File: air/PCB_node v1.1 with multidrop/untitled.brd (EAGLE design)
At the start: 150 x 100 mm, 113 parts, among them J1 10118193-0001LF, J2 10118193-0001LF, K1 351, K2 351, K3 SRD-05VDC-SL-C, K4 351, Q1 MMBT3904, Q10 S9013, Q2 MMBT3904, Q3 12MHz, Q4 S9013, Q5 S9013, Q6 S9013, Q7 12MHz, Q8 MMBT3904, Q9 MMBT3904, U1 CH340G, U10 ADS1115IDGSR, U11 PC817X2NIP0F, U2 ESP32-WROOM-32D, U3 AMS1117, U4 PC817X2NIP0F, U5 PC817X2NIP0F, U6 PC817X2NIP0F, U7 CH340G, U8 AMS1117, U9 ESP32-WROOM-32D, X1 MSTBA2, X2 MSTBA2, X3 MSTBA4, X4 MSTBA3, X5 MSTBA2, X6 MSTBA4, X7 C-GRID-02-70543, X8 MSTBA2

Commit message: menambah GPS chip
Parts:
- added C22: 27nH, rcl:C0805K
- added C23: 10nF, rcl:C0805K
- added D16: SML-LXT0805IW-TR, SML-LXT0805IW-TR:LEDC2012X120N
- added J3: U.FL-R-SMT(01), U.FL-R-SMT_01_:HRS_U.FL-R-SMT(01)
- added Q11: PDTC114EU,115, PDTC114EU_115:SOT65P210X110-3N
- added R32: 10, rcl:M0805
- added R33: 1k, rcl:M0805
- added U12: NEO-M8N-0, NEO-M8N-0:XCVR_NEO-M8N-0
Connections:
- new net N$36: C22.1, C23.1, R32.2
- new net N$37: R32.1, U12.9
- new net N$38: D16.C, Q11.3
- new net N$39: D16.A, R33.1
- new net RF_IN: C22.2, J3.3, U12.11
- new net TIMEPULSE: Q11.1, U12.3
- new net VDD_USB: U12.7
- new net V_BCKP: U12.22
- net GND: now also C23.2, J3.1, J3.2, Q11.2, U12.10, U12.12, U12.13, U12.24
- net RX_GPS: now also U12.21
- net TX_GPS: now also U12.20
- net VCC1: now also R33.2, U12.23
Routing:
- net VCC1: track 168.0 -> 321.5 mm, vias 5 -> 8
- net GND: track 987.7 -> 1077.9 mm, vias 14 -> 17
- net RF_IN: track 0.00 -> 50.8 mm, vias 0 -> 2
- net TX_GPS: track 241.9 -> 271.1 mm, vias 0 -> 1
- net N$37: track 0.00 -> 24.6 mm, vias 0 -> 2
- net TIMEPULSE: track 0.00 -> 23.8 mm
- net RX_GPS: track 246.0 -> 263.4 mm, vias 0 -> 1
- net N$36: track 0.00 -> 14.1 mm, vias 0 -> 2
- net A0: track 92.9 -> 101.9 mm
- net CYBLE2: track 157.7 -> 166.1 mm
- net CYBLE1: track 161.2 -> 169.2 mm
- net CYBLE3: track 120.6 -> 128.5 mm
- net CYBLE5: track 146.1 -> 153.1 mm
- net SCL1: track 286.6 -> 281.6 mm
- net N$38: track 0.00 -> 3.83 mm
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
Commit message: fix PCB
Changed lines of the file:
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@@
 <wire x1="108.07954375" y1="30.049675" x2="105.128484375" y2="30.049675" width="0.2032" layer="1"/>
 <wire x1="105.128484375" y1="30.049675" x2="104.565653125" y2="30.61250625" width="0.2032" layer="1"/>
-<wire x1="104.565653125" y1="30.61250625" x2="104.565653125" y2="33.55030625" width="0.2032" layer="1"/>
-<wire x1="103.640440625" y1="34.47551875" x2="102.309053125" y2="34.47551875" width="0.2032" layer="1"/>
-<wire x1="104.565653125" y1="33.55030625" x2="103.640440625" y2="34.47551875" width="0.2032" layer="1"/>
+<wire x1="104.565653125" y1="30.61250625" x2="104.565653125" y2="33.85510625" width="0.2032" layer="1"/>
+<wire x1="103.945240625" y1="34.47551875" x2="102.309053125" y2="34.47551875" width="0.2032" layer="1"/>
+<wire x1="104.565653125" y1="33.85510625" x2="103.945240625" y2="34.47551875" width="0.2032" layer="1"/>
 <wire x1="120.04408125" y1="34.495728125" x2="115.568690625" y2="34.495728125" width="0.2032" layer="1"/>
 <wire x1="115.568690625" y1="34.495728125" x2="113.475909375" y2="36.588509375" width="0.2032" layer="1"/>
 <wire x1="113.475909375" y1="36.588509375" x2="108.2684125" y2="36.588509375" width="0.2032" layer="1"/>
-<wire x1="106.155421875" y1="34.47551875" x2="103.640440625" y2="34.47551875" width="0.2032" layer="1"/>
+<wire x1="106.155421875" y1="34.47551875" x2="103.945240625" y2="34.47551875" width="0.2032" layer="1"/>
 <wire x1="108.2684125" y1="36.588509375" x2="106.155421875" y2="34.47551875" width="0.2032" layer="1"/>
 <wire x1="136.611259375" y1="7.763196875" x2="132.775103125" y2="7.763196875" width="0.2032" layer="1"/>

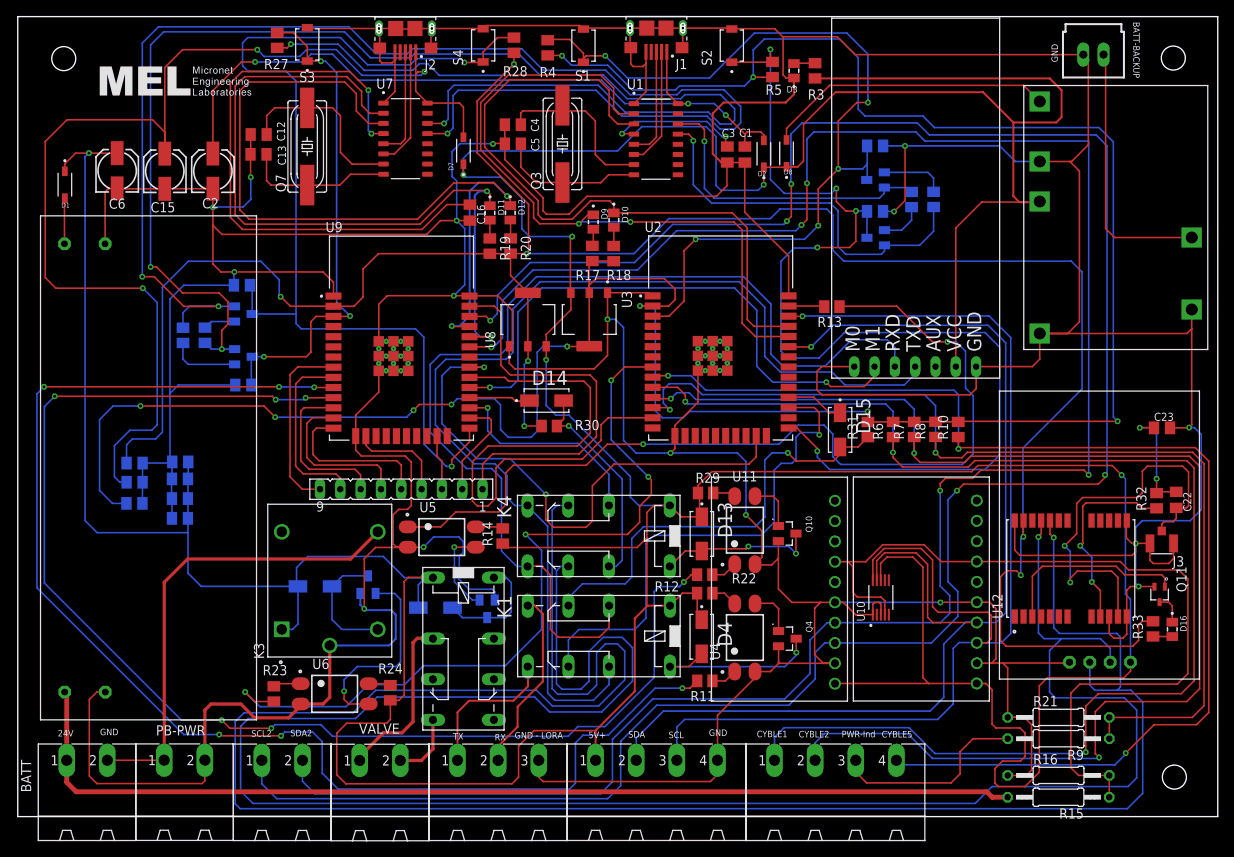
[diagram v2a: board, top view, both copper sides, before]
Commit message: PCB fix dasmeter
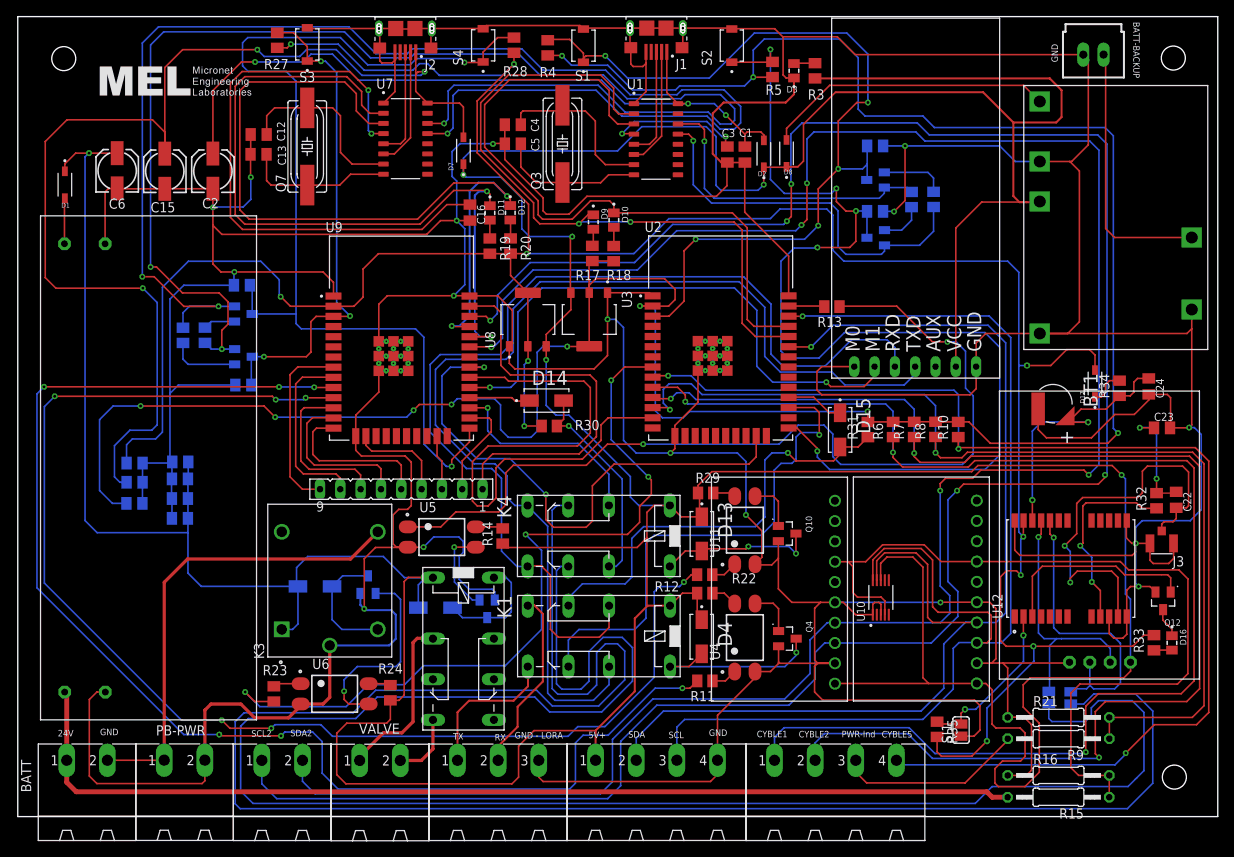
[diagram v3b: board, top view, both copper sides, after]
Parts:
- removed Q11: PDTC114EU,115, PDTC114EU_115:SOT65P210X110-3N
- added BT1: ML414H_IV01E, ML414H_IV01E:SEIKO_ML414H_IV01E
- added C24: 1uF, rcl:C0805K
- added D17: 1N5819HW-7, 1N5819HW-7:SOD3715X145N
- added Q12: S9013, S9013:SOT95P240X120-3N
- added R34: 1k, rcl:M0805
- added R35: 10k, rcl:M0805
- added SJ1, SJ2, SJ3: (no value), jumper:SJ
- moved R33 1.74 mm to (142.2, 24.3)
- moved D16 1.70 mm to (144.4, 24.3)
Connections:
- removed net V_BCKP: U12.22
- new net BACKUP: BT1.1, C24.1, R34.1, U12.22
- new net D_SEL: R35.1, SJ1.2, U12.2
- new net N$41: D17.C, R34.2
- new net RX_GPS1: K4.O2, SJ2.1
- new net TX_GPS1: K4.O1, SJ3.1
- net GND: now also BT1.2, C24.2, Q12.2, SJ1.1; no longer Q11.2
- net N$38: now also Q12.3; no longer Q11.3
- net RX_GPS: now also SJ2.2; no longer K4.O2
- net TIMEPULSE: now also Q12.1; no longer Q11.1
- net TX_GPS: now also SJ3.2; no longer K4.O1
- net VCC1: now also D17.A, R35.2
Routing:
- net TX_GPS1: track 0.00 -> 242.6 mm
- net RX_GPS1: track 0.00 -> 234.8 mm
- net TX_GPS: track 271.1 -> 37.6 mm
- net RX_GPS: track 263.4 -> 32.7 mm
- net GND: track 1077.9 -> 1135.6 mm
- net BACKUP: track 0.00 -> 33.8 mm, vias 0 -> 2
- net VCC1: track 321.5 -> 345.0 mm, vias 8 -> 11
- net D_SEL: track 0.00 -> 20.6 mm, vias 0 -> 2
- net N$41: track 0.00 -> 4.49 mm
- net VCC: track 321.1 -> 324.7 mm
- net OUT+: track 683.2 -> 686.1 mm
- net PB-PWR: track 24.9 -> 23.4 mm
- net TIMEPULSE: track 23.8 -> 25.2 mm
- net SDA1: track 274.7 -> 275.9 mm
- net SCL: track 150.4 -> 149.3 mm
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
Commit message: scada air
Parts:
- removed MODUL-BATT1: (no value), MODUL-BATT:MODUL-BATT
- added D18: US1M-13, US1M-13:DIOM5226X240N
- added K5: 351, relay:351
- added Q11: S9013, S9013:SOT95P240X120-3N
- added R36: 1k, rcl:M0805
- added R37: 10k, rcl:M0805
- added U13: PC817X2NIP0F, PC817X2NIP0F:SOT254P975X400-4N
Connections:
- new net M2_BATT-BACK-SWITCH: R36.2, U9.24
- new net N$40: R37.2, U13.4
- new net N$42: D18.A, K5.16, Q11.3
- new net N$43: Q11.1, U13.3
- new net N$44: K5.S1, X7.2
- net GND: now also Q11.2, U13.2, X7.1; no longer MODUL-BATT1.BATT-, MODUL-BATT1.IN-, MODUL-BATT1.OUT-, X7.2
- net N$29: now also R36.1, U13.1; no longer MODUL-BATT1.BATT+, X7.1
- net OUT+: now also D18.C, K5.1, R37.1; no longer MODUL-BATT1.IN+
- net OUT-BATT: now also K5.P1; no longer MODUL-BATT1.OUT+
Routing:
- net M2_BATT-BACK-SWITCH: track 0.00 -> 268.9 mm, vias 0 -> 6
- net N$42: track 0.00 -> 33.7 mm
- net OUT-BATT: track 36.2 -> 69.1 mm
- net GND: track 1135.6 -> 1104.8 mm, vias 17 -> 19
- net N$29: track 33.1 -> 3.97 mm
- net SCL1: track 281.7 -> 269.4 mm
- net SDA1: track 275.9 -> 263.8 mm
- net N$43: track 0.00 -> 11.9 mm
- net VCC: track 324.7 -> 314.1 mm
- net N$44: track 0.00 -> 8.99 mm
- net VCC1: track 345.0 -> 337.7 mm
- net OUT+: track 686.1 -> 690.7 mm, vias 6 -> 7
- net N$40: track 0.00 -> 4.17 mm
- net N$11: track 113.9 -> 115.4 mm
- net A0: track 101.8 -> 100.5 mm
